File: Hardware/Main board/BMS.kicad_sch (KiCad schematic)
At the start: 24 parts, among them J2 BATT JST, U1 BQ25895

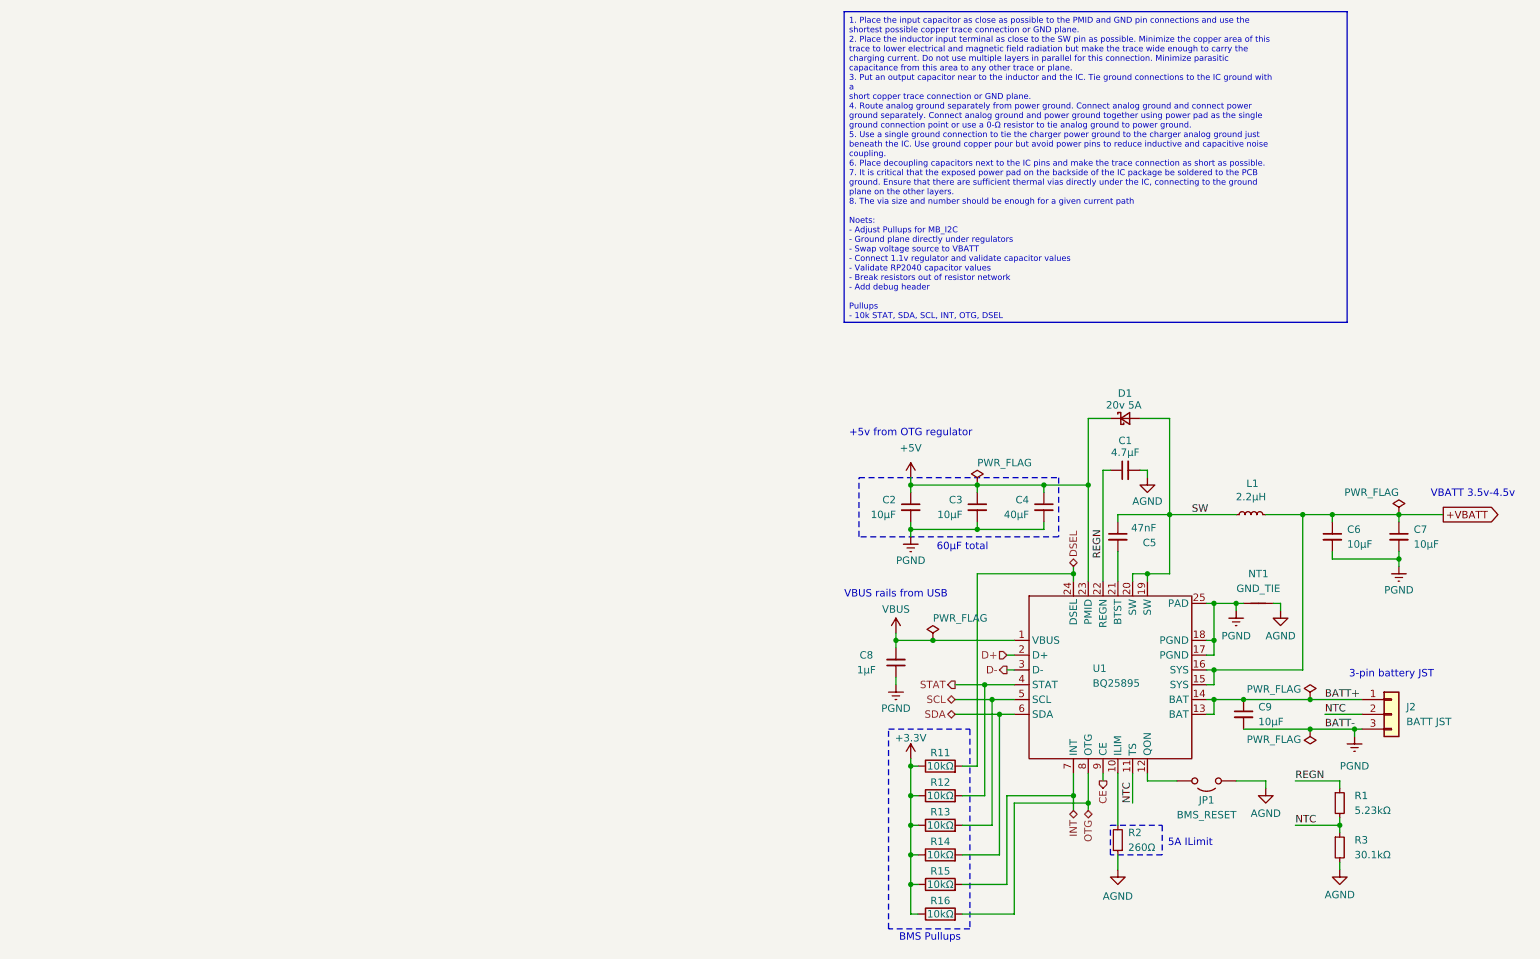
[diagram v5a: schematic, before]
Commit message: Add button and LEDs
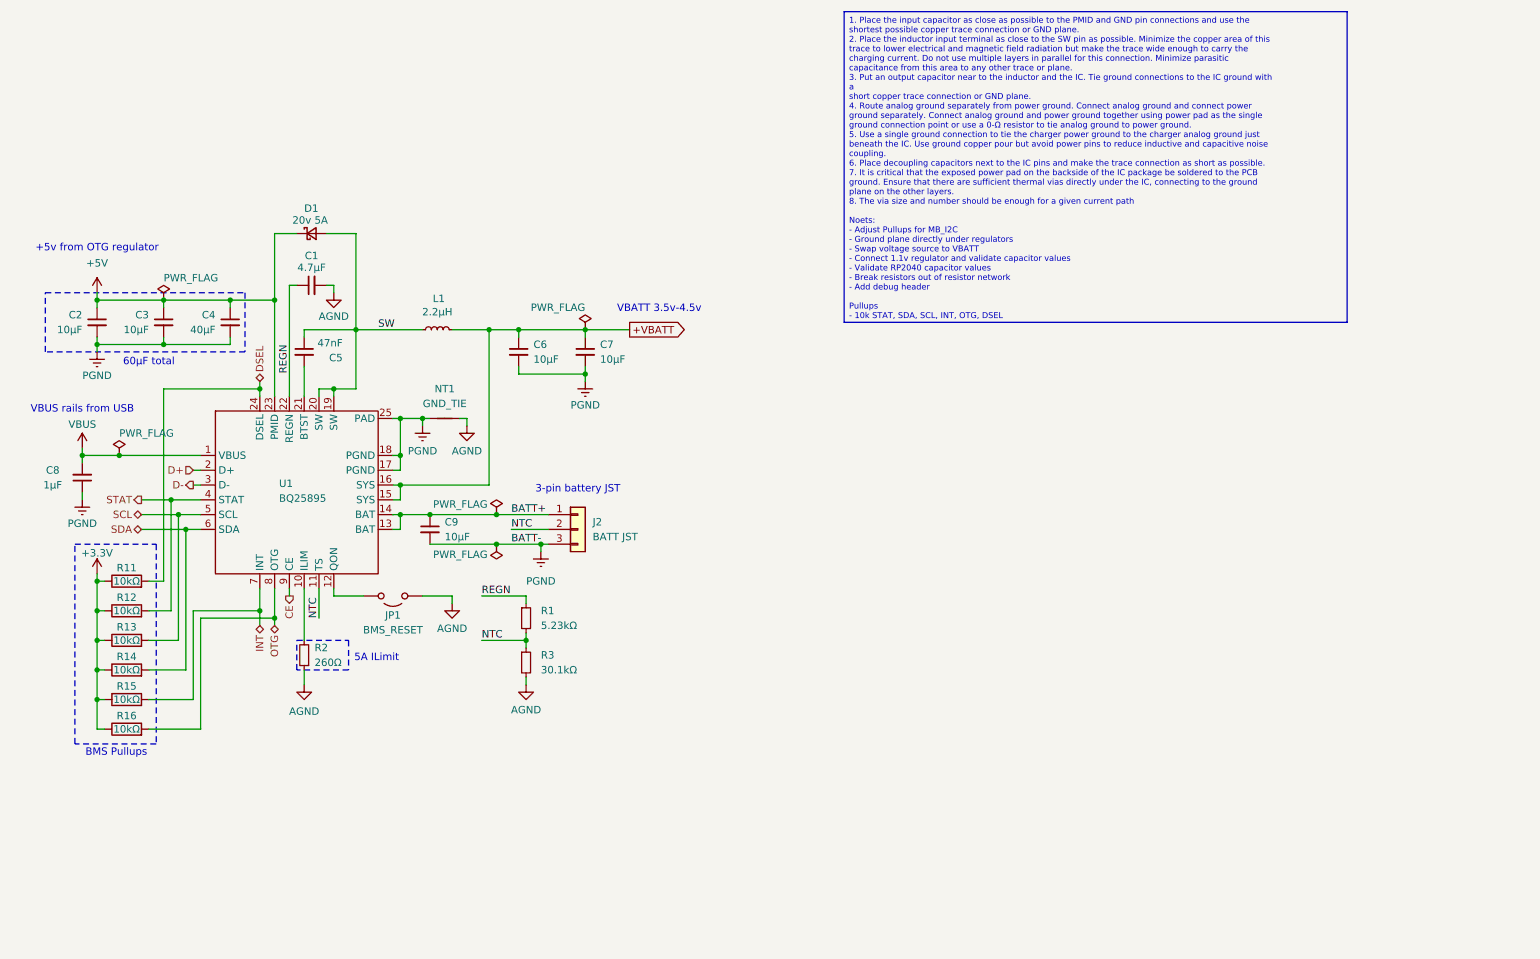
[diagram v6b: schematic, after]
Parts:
- U1: JLCPCB Parts URL (none) -> https://jlcpcb.com/partdetail/TexasInstruments-BQ25895RTWR/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; LCSC Part # (none) -> C80200
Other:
- moved on the sheet: C1, C2, C3, C4, C5, C6, C7, C8, C9, D1, J2, JP1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

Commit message: swap diode footprint + add new part numbers
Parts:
- C4: LCSC Part # (none) -> C426659
- C8: LCSC Part # (none) -> C52923
- D1: footprint Diode_SMD:D_0603_1608Metric -> Diode_SMD:D_SMB; LCSC Part # (none) -> C14651
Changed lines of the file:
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@@
+			)
+		)
+		(property "LCSC Part #" "C52923"
+			(at 135.89 92.71 0)
+			(effects
+				(font
+					(size 1.27 1.27)
+				)
+				(hide yes)
 			)
 		)
@@
 			)
 		)
+		(property "JLCPCB Parts URL" ""
+			(at 161.29 66.04 0)
+			(effects
+				(font
+					(size 1.27 1.27)
+				)
+				(hide yes)
+			)
+		)
+		(property "LCSC Part #" "C426659"
+			(at 161.29 66.04 0)
+			(effects
+				(font
+					(size 1.27 1.27)
+				)
+				(hide yes)
+			)
+		)
 		(pin "2"
 		)
@@
 			)
 		)
-		(property "Footprint" "Diode_SMD:D_0603_1608Metric"
+		(property "Footprint" "Diode_SMD:D_SMB"
 			(at 175.26 50.8 90)
 			(effects
@@
 			(at 175.26 50.8 0)
 			(effects
+				(font
+					(size 1.27 1.27)
+				)
+				(hide yes)
+			)
+		)
+		(property "JLCPCB Parts URL" ""
+			(at 175.26 50.8 0)
+			(effects
+				(font
+					(size 1.27 1.27)
+				)
+				(hide yes)
+			)
+		)
+		(property "LCSC Part #" "C14651"
+			(at 175.26 50.8 0)
+			(effects

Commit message: update ILIM resistor for 250ohm
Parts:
- R2: LCSC Part # (none) -> C861779
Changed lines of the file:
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@@
+			)
+		)
+		(property "JLCPCB Parts URL" ""
+			(at 173.99 123.19 0)
+			(effects
+				(font
+					(size 1.27 1.27)
+				)
+				(hide yes)
+			)
+		)
+		(property "LCSC Part #" "C861779"
+			(at 173.99 123.19 0)
+			(effects
+				(font
+					(size 1.27 1.27)
+				)
+				(hide yes)
 			)
 		)
@@
 			(at 135.89 92.71 0)
 			(effects
+				(font
+					(size 1.27 1.27)
+				)
+				(hide yes)
+			)
+		)
+		(property "JLCPCB Parts URL" ""
+			(at 135.89 92.71 0)
+			(effects
